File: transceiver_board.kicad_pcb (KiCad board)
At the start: 2 copper layers, 212.5 x 77.2 mm, 128 parts, among them J1 85505-5113, J2 Conn_01x01_Male, J3 Laser, J4 Conn_01x01_Male, J5 Receiver Connector, Q1 BC547, Q2 BC547, T1 S558-5999-46-F, U1 LAN83C185-JT, U2 ltc6752ims8-2-pbf, U4 AP63203WU, U5 AP63205WU, U6 LM317_TO-220, U7 LM317_TO-220, Y1 25 MHz

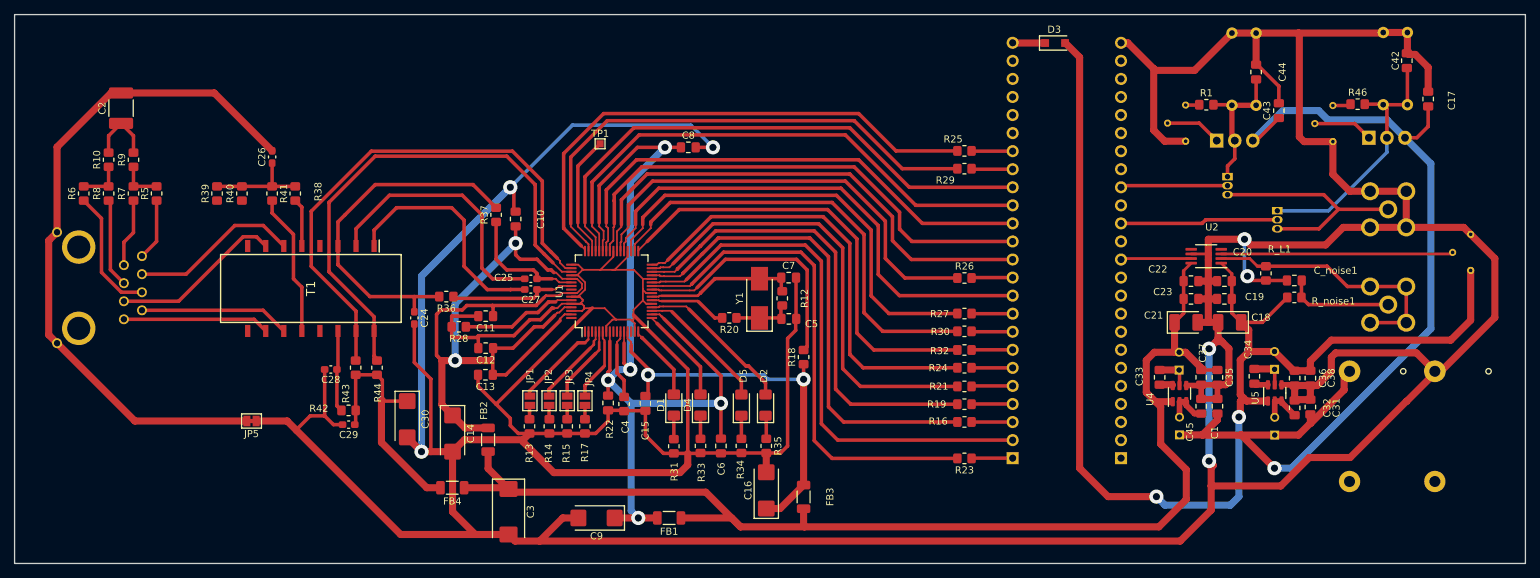
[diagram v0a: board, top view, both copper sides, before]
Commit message: more design review and added ground planes
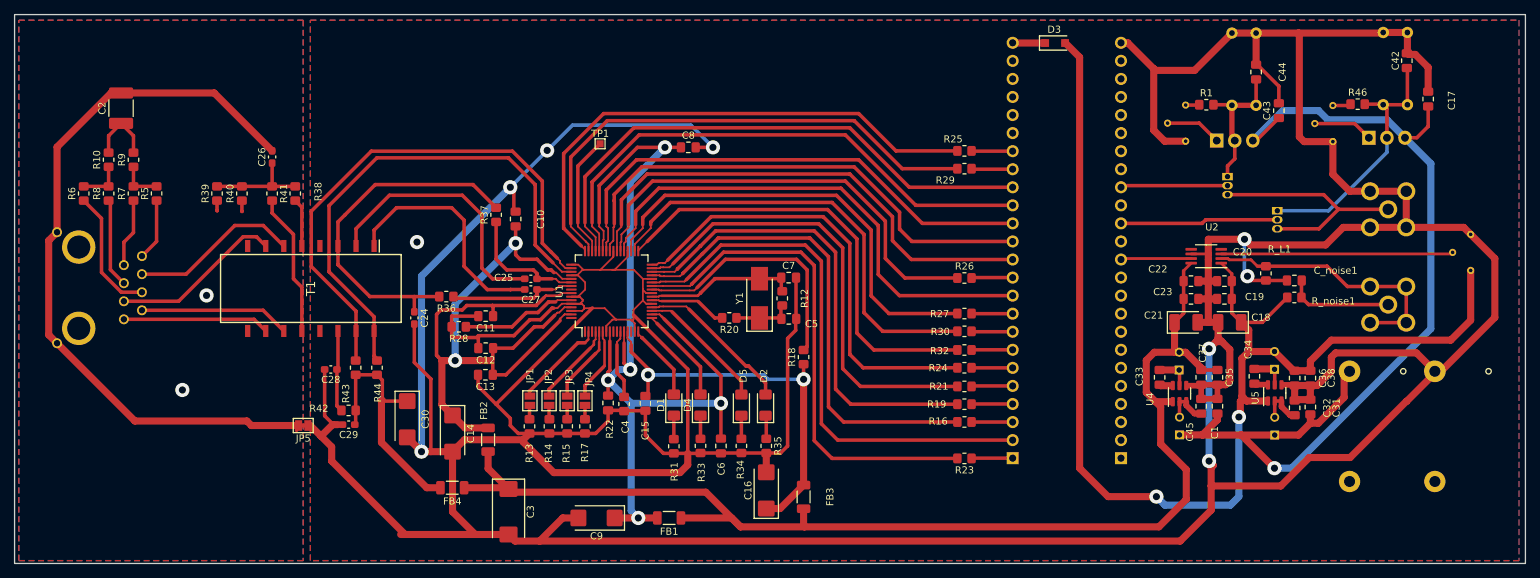
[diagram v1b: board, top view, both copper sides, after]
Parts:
- moved JP5 7.30 mm to (57.0, 99.0)
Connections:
- R39 pad 1: ETH-RXn -> unconnected-(R39-Pad1)
- R40 pad 1: ETH-RXp -> unconnected-(R40-Pad1)
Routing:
- net GND: track 865.4 -> 857.2 mm, vias 7 -> 9
- net GND1: track 96.6 -> 104.2 mm, vias 0 -> 2
- net PHY-AVDD: track 119.4 -> 115.2 mm
- net unconnected-(R40-Pad1): track 0.00 -> 1.55 mm
- net unconnected-(R39-Pad1): track 0.00 -> 1.45 mm
- net +12V: track 135.1 -> 135.7 mm
- added copper zone on B.Cu, net GND
- added copper zone on F.Cu, net GND
- added copper zone on B.Cu, net GND1
- added copper zone on F.Cu, net GND1

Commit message: Move power components slightly further from logic
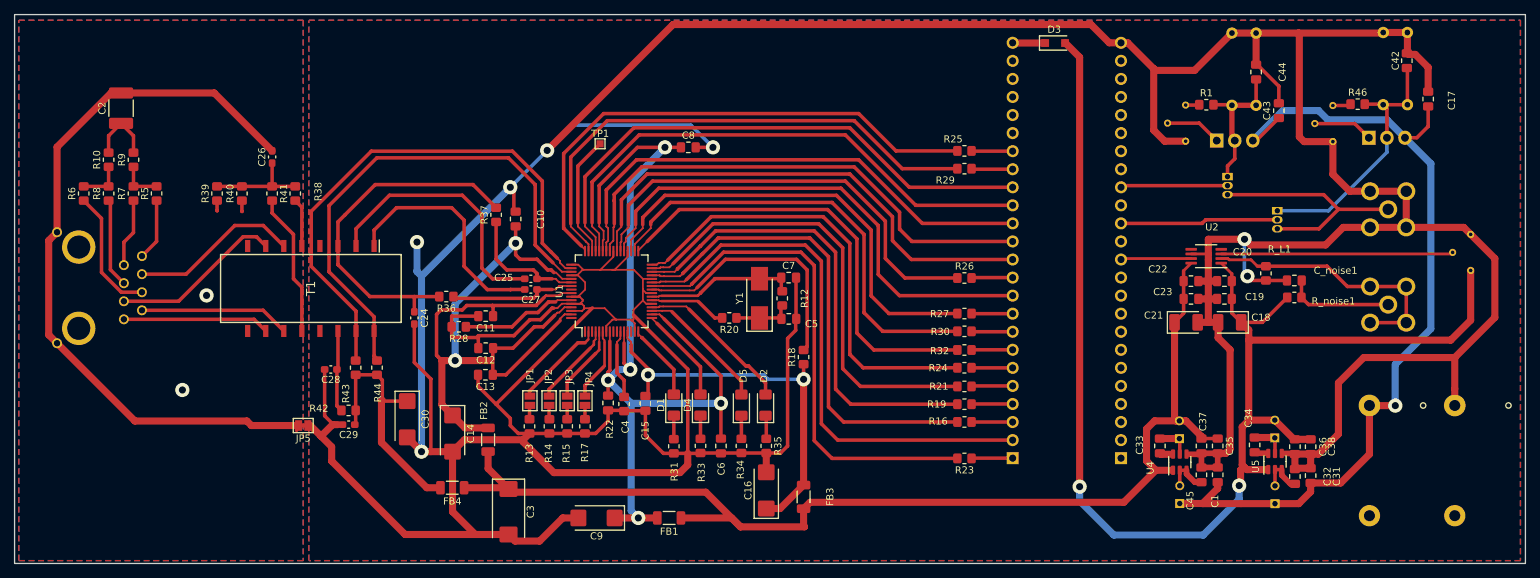
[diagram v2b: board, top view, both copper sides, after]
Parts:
- moved C31 9.65 mm to (198.7, 106.0)
- moved C32 9.65 mm to (196.5, 106.2)
- moved C33 9.65 mm to (177.5, 101.9)
- moved C34 9.65 mm to (190.8, 101.7)
- moved C35 9.65 mm to (185.6, 101.9)
- moved C37 9.65 mm to (183.3, 101.9)
- moved L1 9.65 mm to (180.2, 100.8)
- moved L3 9.65 mm to (180.3, 110.0)
- moved U4 9.65 mm to (180.3, 104.2)
- moved C1 9.65 mm to (185.6, 105.9)
- moved C36 9.65 mm to (196.5, 102.0)
- moved C38 9.65 mm to (198.7, 102.0)
- moved C45 9.65 mm to (183.3, 105.9)
- moved L2 9.65 mm to (193.7, 100.7)
- moved L4 9.65 mm to (193.7, 110.0)
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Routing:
- net GND: track 857.2 -> 812.2 mm, vias 9 -> 7
- net +12V: track 135.7 -> 122.4 mm
- net +5V: track 175.6 -> 188.1 mm
- net +3V3: track 173.0 -> 163.6 mm

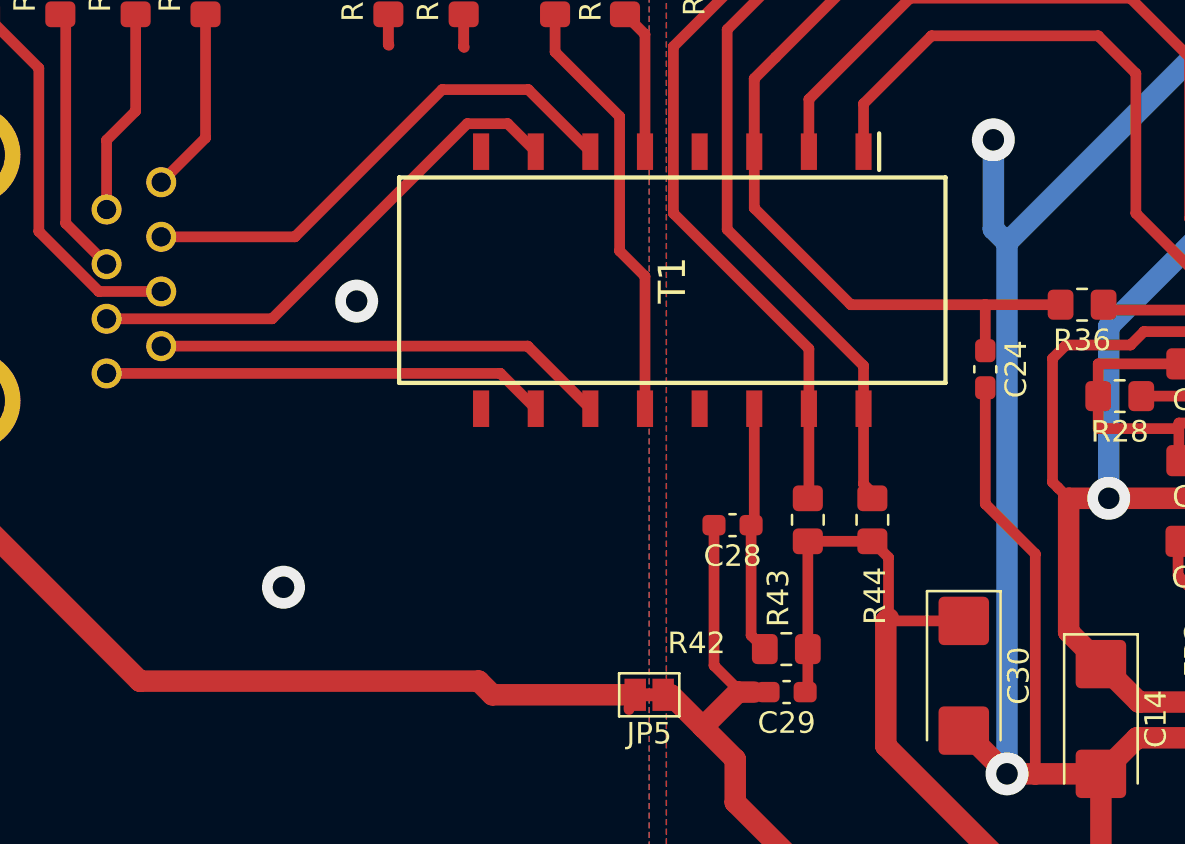
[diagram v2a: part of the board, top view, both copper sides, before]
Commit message: added gnd via thermal relief
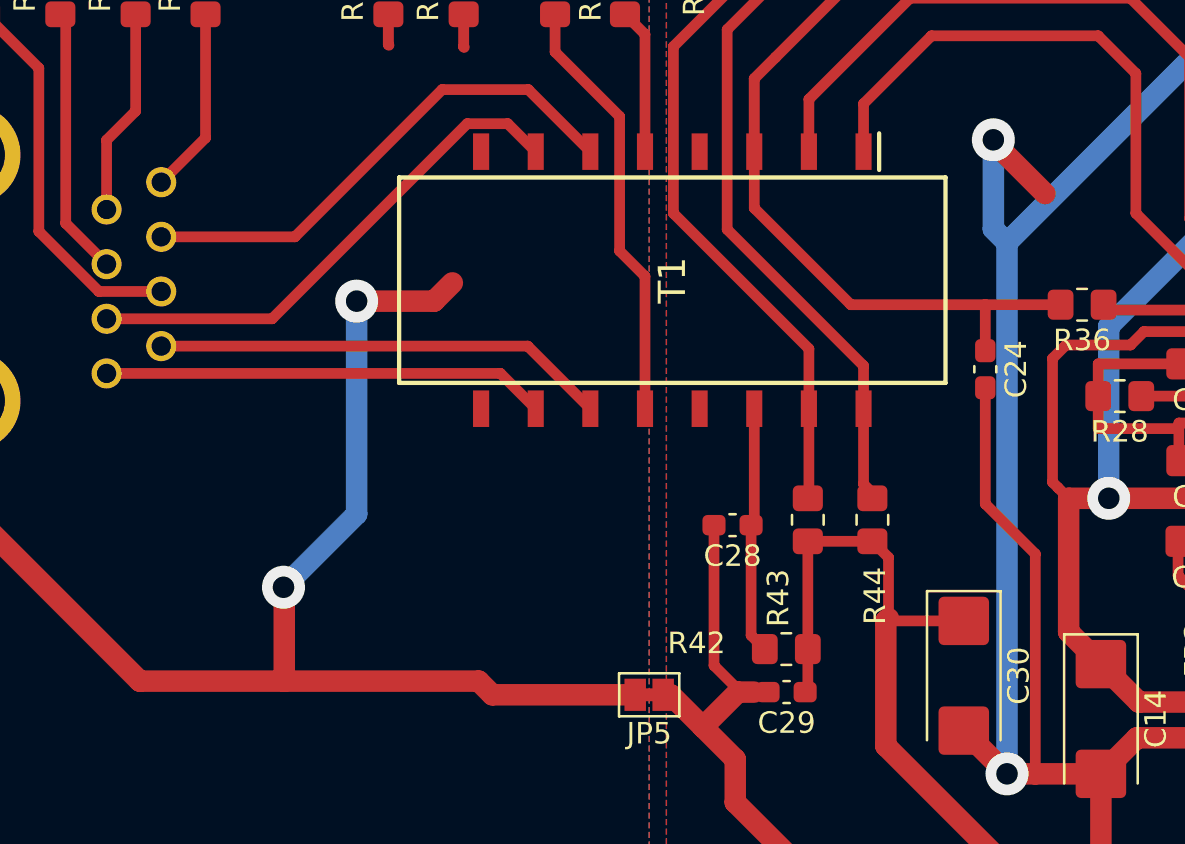
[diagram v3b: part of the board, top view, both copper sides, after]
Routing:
- net GND1: track 104.2 -> 128.0 mm
- net GND: track 812.2 -> 815.7 mm
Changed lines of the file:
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@@
   (segment (start 99.875 98.365) (end 99.875 96.865) (width 0.5) (layer "F.Cu") (net 2))
   (segment (start 122.125 102.865) (end 122.125 105.575) (width 1) (layer "F.Cu") (net 2))
+  (segment (start 73 73.3) (end 75.4 75.7) (width 1) (layer "F.Cu") (net 2))
   (segment (start 105.125 96.915) (end 105.125 100.375) (width 0.5) (layer "F.Cu") (net 2))
   (segment (start 92.75 82.49) (end 93.375 81.865) (width 0.25) (layer "F.Cu") (net 2))
@@
   (segment (start 198.69 103.0155) (end 196.478 103.0155) (width 1) (layer "F.Cu") (net 2))
   (segment (start 111.085 91.085) (end 103.45 83.45) (width 0.5) (layer "F.Cu") (net 2))
+  (segment (start 73 73.2) (end 73 73.3) (width 1) (layer "F.Cu") (net 2))
   (segment (start 98.125 100.115) (end 99.875 98.365) (width 0.5) (layer "F.Cu") (net 2))
   (segment (start 187.3625 102.3125) (end 187.3625 88.3525) (width 1) (layer "F.Cu") (net 2))
@@
   (segment (start 181.8875 75.515) (end 172.155 75.515) (width 0.4) (layer "F.Cu") (net 104))
   (segment (start 172.155 75.515) (end 172.02 75.65) (width 0.4) (layer "F.Cu") (net 104))
+  (segment (start 40.035 98.365) (end 40.035 94.035) (width 1) (layer "F.Cu") (net 133))
+  (segment (start 43.4 80.7) (end 47 80.7) (width 1) (layer "F.Cu") (net 133))
   (segment (start 22.375 59.825) (end 29.9725 52.2275) (width 1) (layer "F.Cu") (net 133))
   (segment (start 31.375 52.2275) (end 44.4875 52.2275) (width 1) (layer "F.Cu") (net 133))
   (segment (start 21.2 86.245) (end 21.2 72.985) (width 1) (layer "F.Cu") (net 133))
-  (segment (start 56.0625 99.5625) (end 56.0625 99.6875) (width 0.5) (layer "F.Cu") (net 133))
   (segment (start 22.375 71.81) (end 22.375 59.825) (width 1) (layer "F.Cu") (net 133))
   (segment (start 29.9725 52.2275) (end 31.375 52.2275) (width 1) (layer "F.Cu") (net 133))
   (segment (start 22.375 87.42) (end 21.2 86.245) (width 1) (layer "F.Cu") (net 133))
+  (segment (start 49.075 98.365) (end 40.035 98.365) (width 1) (layer "F.Cu") (net 133))
+  (segment (start 47 80.7) (end 47.85 79.85) (width 1) (layer "F.Cu") (net 133))
   (segment (start 49.71 99) (end 56.35 99) (width 1) (layer "F.Cu") (net 133))
   (segment (start 49.075 98.365) (end 49.71 99) (width 1) (layer "F.Cu") (net 133))
   (segment (start 21.2 72.985) (end 22.375 71.81) (width 1) (layer "F.Cu") (net 133))
+  (segment (start 40.035 94.035) (end 40 94) (width 1) (layer "F.Cu") (net 133))
+  (segment (start 40.035 98.365) (end 33.32 98.365) (width 1) (layer "F.Cu") (net 133))
   (segment (start 33.32 98.365) (end 22.375 87.42) (width 1) (layer "F.Cu") (net 133))
   (segment (start 44.4875 52.2275) (end 52.625 60.365) (width 1) (layer "F.Cu") (net 133))
-  (segment (start 49.075 98.365) (end 33.32 98.365) (width 1) (layer "F.Cu") (net 133))
   (via (at 43.4 80.7) (size 2) (drill 1) (layers "F.Cu" "B.Cu") (free) (net 133))
   (via (at 40 94) (size 2) (drill 1) (layers "F.Cu" "B.Cu") (free) (net 133))
+  (segment (start 40 94) (end 43.4 90.6) (width 1) (layer "B.Cu") (net 133))
+  (segment (start 43.4 90.6) (end 43.4 80.7) (width 1) (layer "B.Cu") (net 133))
   (segment (start 106.0375 83.9125) (end 106.75 84.625) (width 0.25) (layer "F.Cu") (net 134))
   (segment (start 106.0375 83.875) (end 106.0375 83.9125) (width 0.25) (layer "F.Cu") (net 134))
@@
   (segment (start 48.375 67.365) (end 48.375 68.875) (width 0.508) (layer "F.Cu") (net 143))
   (segment (start 48.375 68.875) (end 48.4 68.9) (width 0.508) (layer "F.Cu") (net 143))
+  (zone (net 0) (net_name "") (layers F&B.Cu) (hatch edge 0.508)
+    (connect_pads (clearance 0))
+    (min_thickness 0.254)
+    (keepout (tracks allowed) (vias allowed) (pads allowed) (copperpour not_allowed) (footprints allowed))
+    (fill (thermal_gap 0.508) (thermal_bridge_width 0.508))
+    (polygon
+      (pts
+        (xy 190.5 76.8)
+        (xy 191 77.1)
+        (xy 191.1 77.8)
+        (xy 191.1 78.3)
+        (xy 190.9 78.9)
+        (xy 190.4 79.2)
+        (xy 189.7 79.3)
+        (xy 189.1 79.1)
+        (xy 188.9 78.9)
+        (xy 188.6 78.5)
+        (xy 188.5 78)
+        (xy 188.8 77.4)
+        (xy 189.2 76.9)
+        (xy 189.8 76.7)
+      )
+    )
+  )
+  (zone (net 0) (net_name "") (layers F&B.Cu) (hatch edge 0.508)
+    (connect_pads (clearance 0))
+    (min_thickness 0.254)
+    (keepout (tracks allowed) (vias allowed) (pads allowed) (copperpour not_allowed) (footprints allowed))
+    (fill (thermal_gap 0.508) (thermal_bridge_width 0.508))
+    (polygon
+      (pts
+        (xy 74.3 101.5)
+        (xy 74.8 101.8)
+        (xy 74.9 102.5)
+        (xy 74.9 103)
+        (xy 74.7 103.6)
+        (xy 74.2 103.9)
+        (xy 73.5 104)
+        (xy 72.9 103.8)
+        (xy 72.7 103.6)
+        (xy 72.4 103.2)
+        (xy 72.3 102.7)
+        (xy 72.6 102.1)
+        (xy 73 101.6)
+        (xy 73.6 101.4)
+      )
+    )
+  )
+  (zone (net 0) (net_name "") (layers F&B.Cu) (hatch edge 0.508)
+    (connect_pads (clearance 0))
+    (min_thickness 0.254)
+    (keepout (tracks allowed) (vias allowed) (pads allowed) (copperpour not_allowed) (footprints allowed))
+    (fill (thermal_gap 0.508) (thermal_bridge_width 0.508))
+    (polygon
+      (pts
+        (xy 91.9 59.1)
+        (xy 92.4 59.4)
+        (xy 92.5 60.1)
+        (xy 92.5 60.6)
+        (xy 92.3 61.2)
+        (xy 91.8 61.5)
+        (xy 91.1 61.6)
+        (xy 90.5 61.4)
+        (xy 90.3 61.2)
+        (xy 90 60.8)
+        (xy 89.9 60.3)
+        (xy 90.2 59.7)
+        (xy 90.6 59.2)
+        (xy 91.2 59)
+      )
+    )
+  )
+  (zone (net 0) (net_name "") (layers F&B.Cu) (hatch edge 0.508)
+    (connect_pads (clearance 0))
+    (min_thickness 0.254)
+    (keepout (tracks allowed) (vias allowed) (pads allowed) (copperpour not_allowed) (footprints allowed))
+    (fill (thermal_gap 0.508) (thermal_bridge_width 0.508))
+    (polygon
+      (pts
+        (xy 190 71.6)
+        (xy 190.5 71.9)
+        (xy 190.6 72.6)
+        (xy 190.6 73.1)
+        (xy 190.4 73.7)
+        (xy 189.9 74)
+        (xy 189.2 74.1)
+        (xy 188.6 73.9)
+        (xy 188.4 73.7)
+        (xy 188.1 73.3)
+        (xy 188 72.8)
+        (xy 188.3 72.2)
+        (xy 188.7 71.7)
+        (xy 189.3 71.5)
+      )
+    )
+  )
   (zone (net 133) (net_name "GND1") (layers F&B.Cu) (hatch edge 0.508)
     (connect_pads (clearance 0.508))
@@
         (xy 17 42)
         (xy 57 42)
+      )
+    )
+  )
+  (zone (net 0) (net_name "") (layers F&B.Cu) (hatch edge 0.508)
+    (connect_pads (clearance 0))
+    (min_thickness 0.254)
+    (keepout (tracks allowed) (vias allowed) (pads allowed) (copperpour not_allowed) (footprints allowed))
+    (fill (thermal_gap 0.508) (thermal_bridge_width 0.508))
+    (polygon
+      (pts
+        (xy 44 79.5)
+        (xy 44.5 79.8)
+        (xy 44.6 80.5)
+        (xy 44.6 81)
+        (xy 44.4 81.6)
+        (xy 43.9 81.9)
+        (xy 43.2 82)
+        (xy 42.6 81.8)
+        (xy 42.4 81.6)
+        (xy 42.1 81.2)
+        (xy 42 80.7)
+        (xy 42.3 80.1)
+        (xy 42.7 79.6)
+        (xy 43.3 79.4)
+      )
+    )
+  )
+  (zone (net 0) (net_name "") (layers F&B.Cu) (hatch edge 0.508)
+    (connect_pads (clearance 0))
+    (min_thickness 0.254)
+    (keepout (tracks allowed) (vias allowed) (pads allowed) (copperpour not_allowed) (footprints allowed))
+    (fill (thermal_gap 0.508) (thermal_bridge_width 0.508))
+    (polygon
+      (pts
+        (xy 40.6 92.8)
+        (xy 41.1 93.1)
+        (xy 41.2 93.8)
+        (xy 41.2 94.3)
+        (xy 41 94.9)
+        (xy 40.5 95.2)
+        (xy 39.8 95.3)
+        (xy 39.2 95.1)
+        (xy 39 94.9)
+        (xy 38.7 94.5)
+        (xy 38.6 94)
+        (xy 38.9 93.4)
+        (xy 39.3 92.9)
+        (xy 39.9 92.7)
       )
     )
@@
       )
     )
+  )
+  (zone (net 0) (net_name "") (layers F&B.Cu) (hatch edge 0.508)
+    (connect_pads (clearance 0))
+    (min_thickness 0.254)
+    (keepout (tracks allowed) (vias allowed) (pads allowed) (copperpour not_allowed) (footprints allowed))
+    (fill (thermal_gap 0.508) (thermal_bridge_width 0.508))
+    (polygon
+      (pts
+        (xy 73.6 72)
+        (xy 74.1 72.3)
+        (xy 74.2 73)
+        (xy 74.2 73.5)
+        (xy 74 74.1)
+        (xy 73.5 74.4)
+        (xy 72.8 74.5)
+        (xy 72.2 74.3)
+        (xy 72 74.1)
+        (xy 71.7 73.7)
+        (xy 71.6 73.2)
+        (xy 71.9 72.6)
+        (xy 72.3 72.1)
+        (xy 72.9 71.9)
+      )
+    )
+  )
+  (zone (net 0) (net_name "") (layers F&B.Cu) (hatch edge 0.508)
+    (connect_pads (clearance 0))
+    (min_thickness 0.254)
+    (keepout (tracks allowed) (vias allowed) (pads allowed) (copperpour not_allowed) (footprints allowed))
+    (fill (thermal_gap 0.508) (thermal_bridge_width 0.508))
+    (polygon
+      (pts
+        (xy 115.2 58.7)
+        (xy 115.7 59)
+        (xy 115.8 59.7)
+        (xy 115.8 60.2)
+        (xy 115.6 60.8)
+        (xy 115.1 61.1)
+        (xy 114.4 61.2)
+        (xy 113.8 61)
+        (xy 113.6 60.8)
+        (xy 113.3 60.4)
+        (xy 113.2 59.9)
+        (xy 113.5 59.3)
+        (xy 113.9 58.8)
+        (xy 114.5 58.6)
+      )
+    )
+  )
+  (zone (net 0) (net_name "") (layers F&B.Cu) (hatch edge 0.508)
+    (connect_pads (clearance 0))
+    (min_thickness 0.254)
+    (keepout (tracks allowed) (vias allowed) (pads allowed) (copperpour not_allowed) (footprints allowed))
+    (fill (thermal_gap 0.508) (thermal_bridge_width 0.508))
+    (polygon
+      (pts
+        (xy 86.7 64.3)
+        (xy 87.2 64.6)
+        (xy 87.3 65.3)
+        (xy 87.3 65.8)
+        (xy 87.1 66.4)
+        (xy 86.6 66.7)
+        (xy 85.9 66.8)
+        (xy 85.3 66.6)
+        (xy 85.1 66.4)
+        (xy 84.8 66)
+        (xy 84.7 65.5)
+        (xy 85 64.9)
+        (xy 85.4 64.4)
+        (xy 86 64.2)
+      )
+    )
